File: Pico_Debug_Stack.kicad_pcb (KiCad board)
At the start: 4 copper layers, 43 x 98 mm, 146 parts, among them J1 Stack to Motherboard Connector, J10 USB_A, J2 Scope_TP, J3 BM03B-SRSS-TB, J4 Conn_01x04_Pin, J7 Conn_01x04, J8 Scope_TP_21-40, SW2 Tactile Button, 160gf, SW3 Tactile Button, 160gf, SW4 Tactile Button, 160gf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

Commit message: Replace wrong version with Version 0.1.1
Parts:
- moved TP1 38.1 mm to (128.2, 101.1)
- moved TP2 38.0 mm to (91.2, 101.3)
- moved TP4 34.0 mm to (91.2, 64.3)
- moved R47 0.26 mm to (105.1, 95.0)
- moved C48 0.21 mm to (116.1, 133.4)
- moved C49 0.20 mm to (130.2, 136.1)
- moved R52 0.20 mm to (130.2, 133.4)
- moved D3 0.19 mm to (97.3, 155.8)
- moved R36 0.15 mm to (124.7, 145.9)
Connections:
- C6 pad 1: unconnected-(C6-Pad1) -> Net-(U3-RESET)
- C6 pad 2: unconnected-(C6-Pad2) -> GND
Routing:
- net GND: track 9.87 -> 1700.4 mm, vias 4 -> 84
- net +3V3: track 25.2 -> 1598.2 mm, vias 3 -> 59
- net Net-(SW4-B): track 4.07 -> 96.7 mm, vias 0 -> 2
- net Net-(U2-GPIO36): track 18.6 -> 103.4 mm, vias 2 -> 4
- net /RUN: track 28.6 -> 110.9 mm
- net Net-(U2-GPIO37): track 15.5 -> 91.2 mm
- net Net-(U2-GPIO43_ADC3): track 5.86 -> 81.2 mm
- net Net-(U2-GPIO35): track 22.0 -> 77.7 mm
- net 3V3P: track 10.8 -> 54.9 mm, vias 1 -> 5
- net Net-(U2-GPIO6): track 0.00 -> 43.6 mm, vias 0 -> 2
- net Net-(SW6-B): track 0.00 -> 41.9 mm, vias 0 -> 2
- net Net-(U2-GPIO21): track 55.4 -> 27.9 mm
- net Net-(U2-QSPI_SS): track 0.00 -> 26.8 mm, vias 0 -> 2
- net /GPIO1: track 45.1 -> 71.7 mm, vias 5 -> 3
- net /GPIO0: track 49.0 -> 71.9 mm, vias 4 -> 5
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- added copper zone on In2.Cu, net +3V3
- added copper zone on B.Cu, net GND
- added copper zone on F.Cu, net GND
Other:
- board text added: "BOOT"
- board text added: "DUT"
- board text added: "Logic Anal."
- board text added: "Probe"
- board text added: "RST"
- board text added: "RUN"
- board text added: "SWCK"
- board text added: "SWIO"
- board text added: "Version 0.1.1"
- board text added: "Walla Walla University School of Engineering 2025"
- board text removed: "BT"
- board text removed: "CK"
- board text removed: "LA"
- board text removed: "PRB"
- board text removed: "RS"
- board text removed: "SW"
- board text removed: "Walla Walla University Engineering 2025"

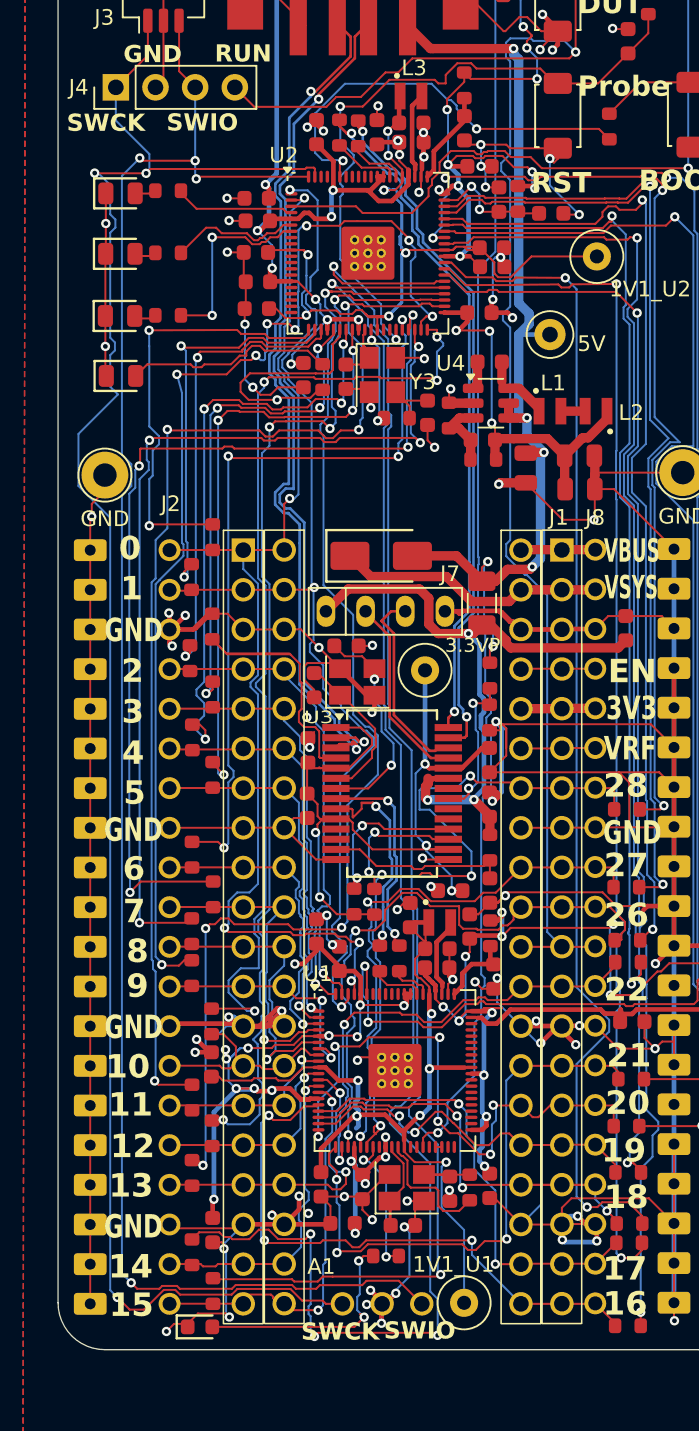
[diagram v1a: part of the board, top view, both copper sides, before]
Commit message: Added a power plate for 1V1_U1 and 1V1_U2 to the power layer
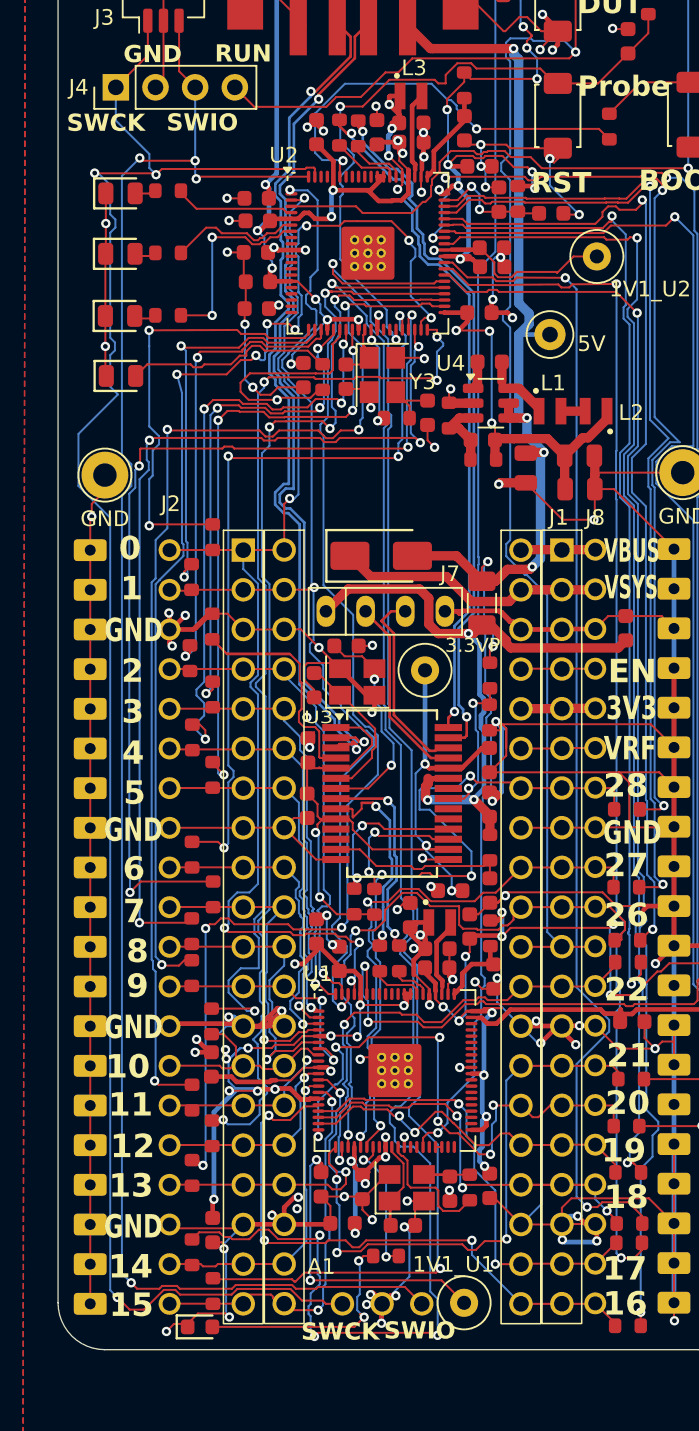
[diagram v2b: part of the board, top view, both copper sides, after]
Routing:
- net GND: track 1700.4 -> 1751.9 mm
- net +3V3: track 1598.2 -> 1566.2 mm
- net +1V1_U1: track 56.5 -> 77.5 mm, vias 6 -> 8
- net +1V1_U2: track 71.4 -> 74.7 mm, vias 7 -> 9
- net Net-(U2-GPIO36): track 103.4 -> 105.4 mm
- net /GPIO28: track 47.3 -> 46.3 mm
- net /D4+: track 43.4 -> 44.2 mm
- net Net-(U2-GPIO37): track 91.2 -> 91.9 mm
- net /D4-: track 44.5 -> 45.2 mm
- net Net-(U2-GPIO28): track 48.3 -> 49.0 mm
- net /D2+: track 56.9 -> 57.4 mm
- net /GPIO0: track 71.9 -> 72.5 mm
- net /D2-: track 57.1 -> 57.7 mm
- added copper zone on In2.Cu, net +1V1_U1
- added copper zone on In2.Cu, net +1V1_U2

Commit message: Added a power plate for 1V1_U1 and 1V1_U2 to the power layer
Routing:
- net +3V3: track 1566.2 -> 1625.2 mm
- net +1V1_U1: track 77.5 -> 82.1 mm
